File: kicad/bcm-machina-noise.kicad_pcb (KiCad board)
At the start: 2 copper layers, 125.2 x 78 mm, 70 parts, among them J2 AVR-ISP-6, J3 AudioJack2_SwitchT, J4 USB_B_Micro, J5 AudioJack2_SwitchT, Q1 J113, Q2 J113, SW1 SW_Push, SW2 SW_Push, U1 4069, U2 MCP602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

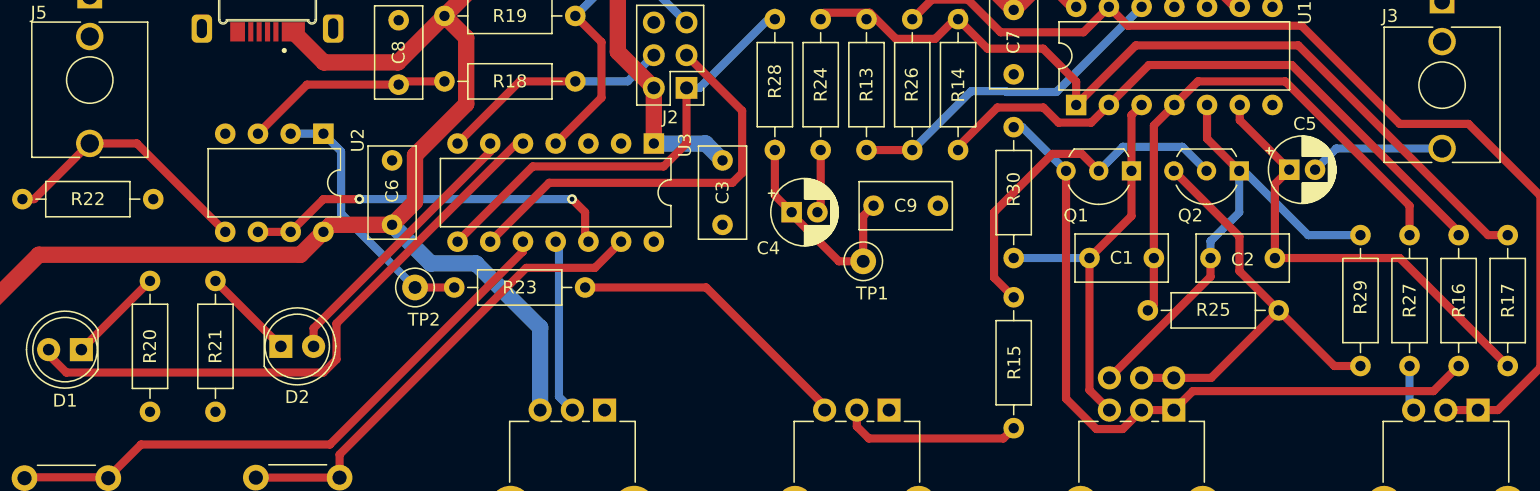
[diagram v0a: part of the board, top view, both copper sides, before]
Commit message: Tweaks to circuitry
Fixing bugs
Changing some values
Adding another potentiometer
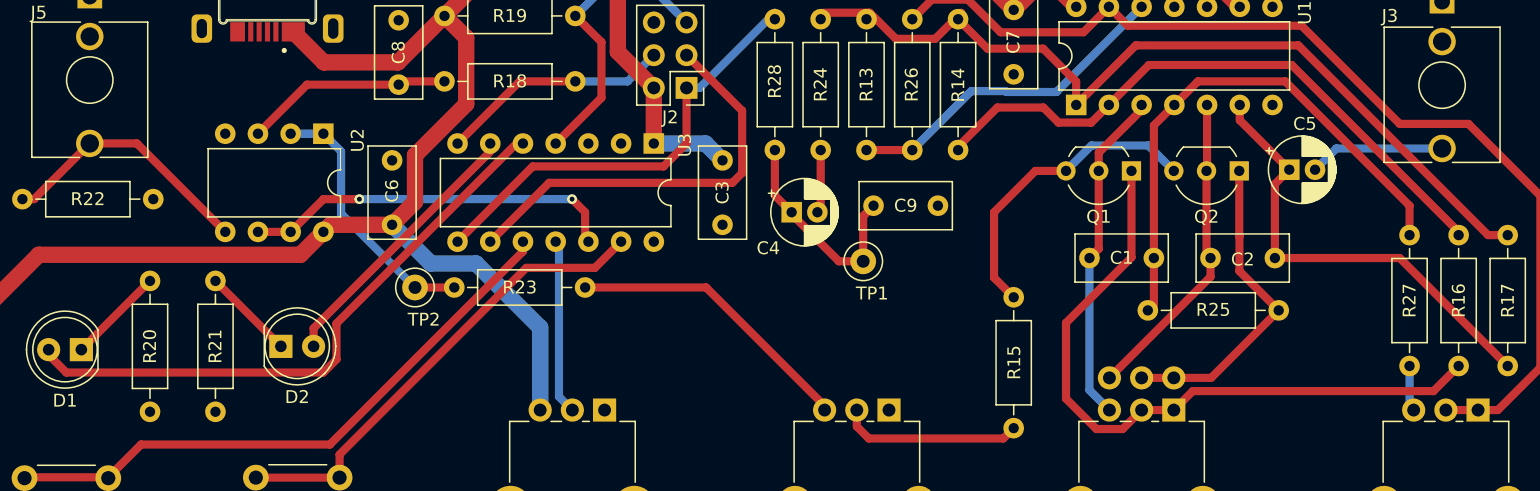
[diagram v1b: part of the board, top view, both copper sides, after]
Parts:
- removed R29, R30: 100k, Resistor_THT:R_Axial_DIN0207_L6.3mm_D2.5mm_P10.16mm_Horizontal
- Q1, Q2: value J113 -> Q_NJFET_DSG; footprint Package_TO_SOT_THT:TO-92L_Inline_Wide -> Rumblesan_Standard_Parts:TO-92_Inline_Wide
- R16, R25: value 1k -> 47r
- RV1: value 100k -> 10k
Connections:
- C1 pad 1: Net-(Q1-D) -> Net-(Q1-S)
- C2 pad 1: Net-(Q2-D) -> Net-(Q2-S)
- Q1 pad 2: Net-(Q1-G) -> Net-(Q1-S)
- Q1 pad 3: Net-(Q1-S) -> Net-(Q1-G)
- Q2 pad 2: Net-(Q1-G) -> Net-(Q2-S)
- Q2 pad 3: Net-(Q2-S) -> Net-(Q1-G)
- R16 pad 2: Net-(Q1-S) -> Net-(Q1-D)
- R25 pad 2: Net-(Q2-S) -> Net-(Q2-D)
- RV1 pad 1: Net-(Q1-S) -> Net-(Q1-D)
- RV1 pad 2: Net-(Q1-S) -> Net-(Q1-D)
- RV1 pad 3: Net-(Q1-D) -> Net-(Q1-S)
- RV1 pad 4: Net-(Q2-S) -> Net-(Q2-D)
- RV1 pad 5: Net-(Q2-S) -> Net-(Q2-D)
- RV1 pad 6: Net-(Q2-D) -> Net-(Q2-S)
- U1 pad 3: Net-(Q1-D) -> Net-(Q1-S)
- U1 pad 5: Net-(Q2-D) -> Net-(Q2-S)
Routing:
- net Net-(Q1-S): track 56.6 -> 25.6 mm
- net Net-(Q1-D): track 31.9 -> 53.3 mm
- net Net-(Q2-D): track 37.9 -> 24.9 mm
- net Net-(Q2-S): track 35.2 -> 24.1 mm
- net Net-(Q1-G): track 27.7 -> 24.2 mm
- net Net-(R14-Pad2): track 48.3 -> 47.8 mm

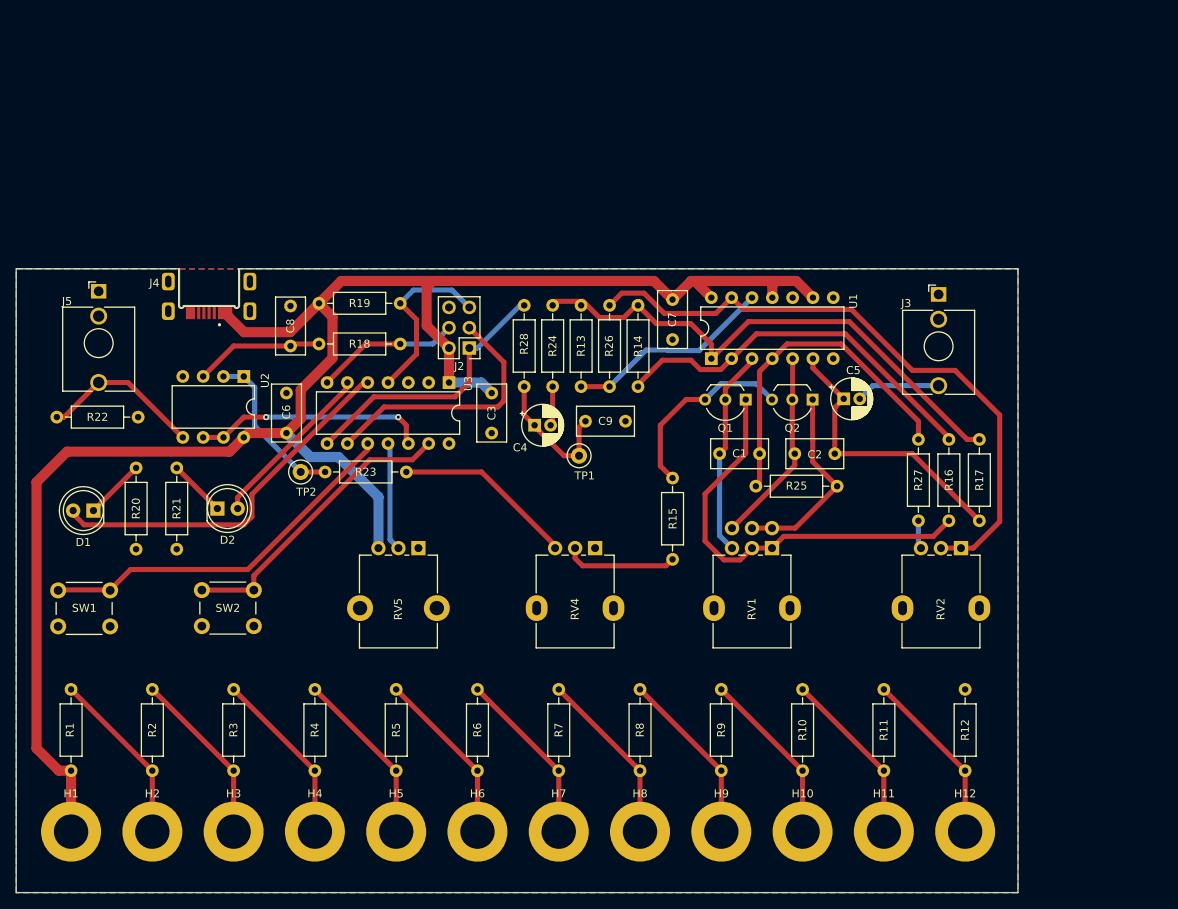
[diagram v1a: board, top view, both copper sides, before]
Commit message: new Yorick PCB created with SVG graphics
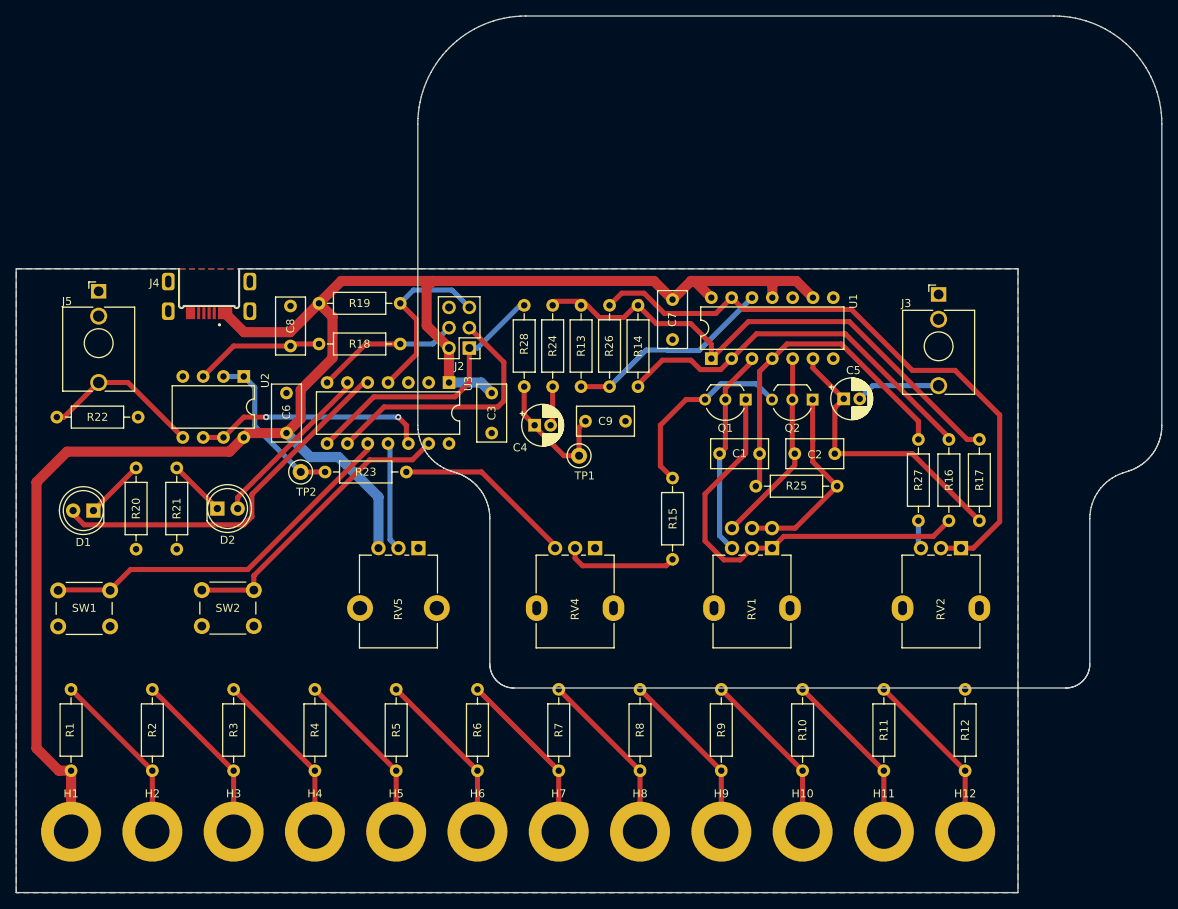
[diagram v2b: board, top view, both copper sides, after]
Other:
- board size 125.2 x 78 mm -> 143.2 x 109.6 mm
